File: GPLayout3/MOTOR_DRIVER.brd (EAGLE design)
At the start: 169.2 x 45.4 mm, 95 parts, among them T1 2N2222, T2 2N2222, U7 ATMEGA328P_TQFP, Y1 16MHz

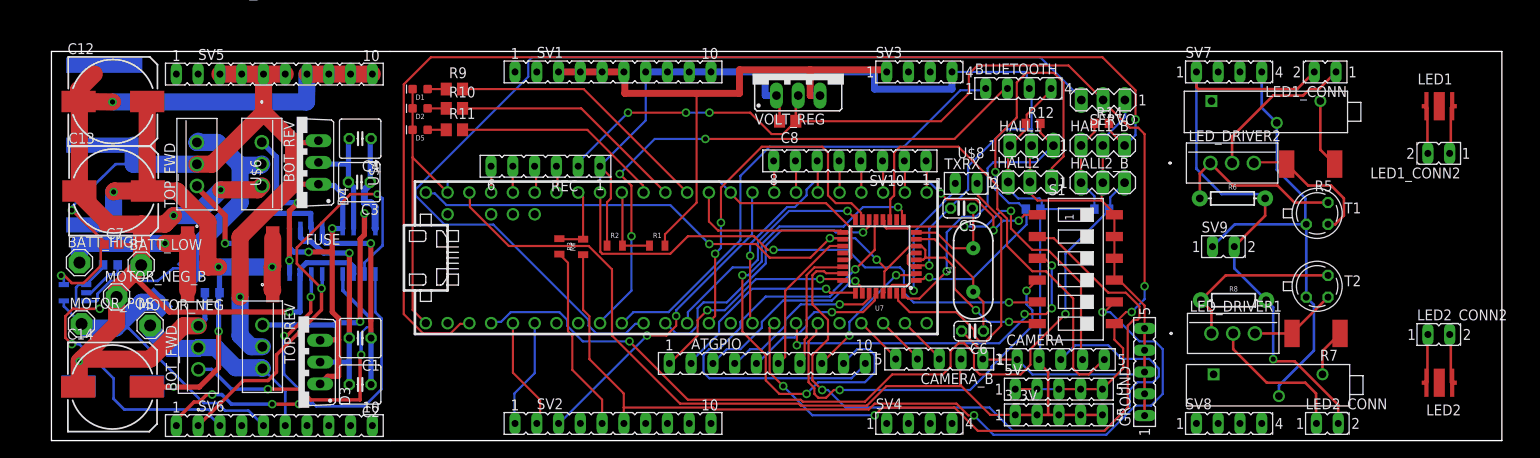
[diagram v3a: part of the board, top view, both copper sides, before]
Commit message: added several resistor values
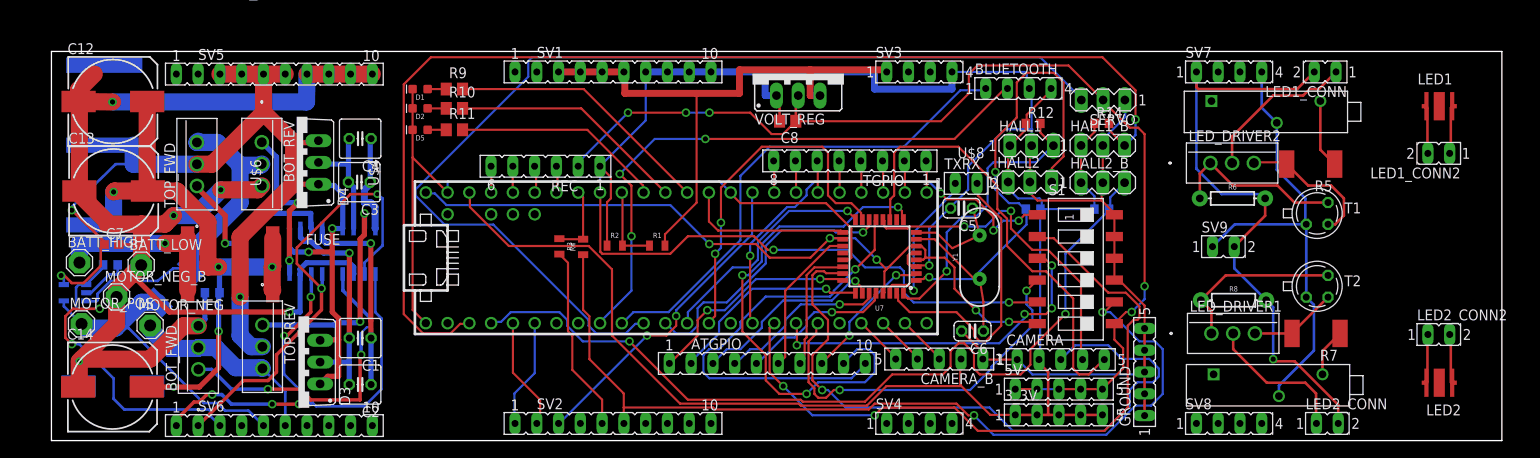
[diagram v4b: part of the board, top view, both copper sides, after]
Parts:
- R10, R11, R9: value (none) -> 59
- R5, R7: value (none) -> 1
- moved Y1 1.68 mm to (108.3, 21.4)
- renumbered SV10 to TGPIO
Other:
- outline, holes or cut-outs redrawn
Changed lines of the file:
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@@
 <?xml version="1.0" encoding="utf-8"?>
 <!DOCTYPE eagle SYSTEM "eagle.dtd">
-<eagle version="8.0.0">
+<eagle version="8.0.1">
 <drawing>
 <settings>
@@
 <board>
 <plain>
-<wire x1="0" y1="0" x2="39.5" y2="0" width="0" layer="20"/>
-<wire x1="39.5" y1="0" x2="169.17" y2="0" width="0" layer="20"/>
+<wire x1="0" y1="0" x2="169.17" y2="0" width="0" layer="20"/>
 <wire x1="169.17" y1="0" x2="169.17" y2="45.39" width="0" layer="20"/>
-<wire x1="169.17" y1="45.39" x2="39.5" y2="45.39" width="0" layer="20"/>
+<wire x1="169.17" y1="45.39" x2="0" y2="45.39" width="0" layer="20"/>
 <dimension x1="39.5" y1="0" x2="130.94" y2="0" x3="85.22" y3="-29.21" textsize="1.778" layer="48" unit="inch"/>
-<wire x1="39.5" y1="45.39" x2="0" y2="45.39" width="0" layer="20"/>
 <wire x1="0" y1="45.39" x2="0" y2="0" width="0" layer="20"/>
 <dimension x1="1" y1="45.54" x2="1" y2="-0.18" x3="-6.62" y3="22.68" textsize="1.778" layer="48" unit="inch"/>
@@
 <attribute name="PRICE" value="$1.38" x="96.578" y="21.482" size="1.778" layer="27" rot="R180" display="off"/>
 </element>
-<element name="Y1" library="SparkFun-Clocks" package="HC49US" value="16MHz" x="107.515" y="19.9" rot="R90">
-<attribute name="DIGIKEY_PART_NUMBER" value="887-2425-1-ND" x="107.515" y="19.9" size="1.778" layer="27" rot="R90" display="off"/>
-<attribute name="MANUFACTURER" value="TXC CORPORATION" x="107.515" y="19.9" size="1.778" layer="27" rot="R90" display="off"/>
-<attribute name="MANUFACTURER_PART_NUMBER" value="9C-16.000MBBK-T" x="107.515" y="19.9" size="1.778" layer="27" rot="R90" display="off"/>
-<attribute name="PRICE" value="$0.36" x="107.515" y="19.9" size="1.778" layer="27" rot="R90" display="off"/>
+<element name="Y1" library="SparkFun-Clocks" package="HC49US" value="16MHz" x="108.265" y="21.4" rot="R90">
+<attribute name="DIGIKEY_PART_NUMBER" value="887-2425-1-ND" x="108.265" y="21.4" size="1.778" layer="27" rot="R90" display="off"/>
+<attribute name="MANUFACTURER" value="TXC CORPORATION" x="108.265" y="21.4" size="1.778" layer="27" rot="R90" display="off"/>
+<attribute name="MANUFACTURER_PART_NUMBER" value="9C-16.000MBBK-T" x="108.265" y="21.4" size="1.778" layer="27" rot="R90" display="off"/>
+<attribute name="PRICE" value="$0.36" x="108.265" y="21.4" size="1.778" layer="27" rot="R90" display="off"/>
 </element>
 <element name="SV1" library="con-lsta" package="FE10" value="" x="65.5" y="43"/>
@@
 </element>
 <element name="U$7" library="ledpot" package="POT" value="POT" x="132.125" y="40.75" rot="R270"/>
-<element name="R5" library="rcl" package="R2512" value="" x="146.875" y="32.25" rot="R180"/>
+<element name="R5" library="rcl" package="R2512" value="1" x="146.875" y="32.25" rot="R180"/>
 <element name="T1" library="transistor" package="TO18" value="2N2222" x="147.625" y="26.5"/>
 <element name="R6" library="SparkFun-Resistors" package="AXIAL-0.3" value="1k" x="137.75" y="28.25">
@@
 </element>
 <element name="U$3" library="ledpot" package="POT" value="POT" x="132.375" y="8.875" rot="R270"/>
-<element name="R7" library="rcl" package="R2512" value="" x="147.5" y="12.5" rot="R180"/>
+<element name="R7" library="rcl" package="R2512" value="1" x="147.5" y="12.5" rot="R180"/>
 <element name="T2" library="transistor" package="TO18" value="2N2222" x="147.625" y="18"/>
 <element name="R8" library="SparkFun-Resistors" package="AXIAL-0.3" value="1k" x="137.875" y="16.375">
@@
 <element name="3_3V" library="con-lsta" package="FE05-1" value="" x="117.5" y="3"/>
 <element name="5V" library="con-lsta" package="FE05-1" value="" x="117.5" y="6"/>
-<element name="R9" library="rcl" package="R0805" value="" x="47" y="41"/>
-<element name="R10" library="rcl" package="R0805" value="" x="47" y="38.75"/>
-<element name="R11" library="rcl" package="R0805" value="" x="47" y="36.25"/>
+<element name="R9" library="rcl" package="R0805" value="59" x="47" y="41"/>
+<element name="R10" library="rcl" package="R0805" value="59" x="47" y="38.75"/>
+<element name="R11" library="rcl" package="R0805" value="59" x="47" y="36.25"/>
 <element name="D1" library="SparkFun-LED" package="LED-0603" value="" x="43" y="41" rot="R180"/>
 <element name="D2" library="SparkFun-LED" package="LED-0603" value="" x="43" y="38.75" rot="R180"/>
@@
 <element name="ATGPIO" library="con-lsta" package="FE10" value="" x="83.5" y="9"/>
 <element name="R17" library="rcl" package="R2512" value="10m" x="14.394540625" y="18.11175" rot="MR315"/>
-<element name="SV10" library="con-lsta" package="FE08" value="" x="93.125" y="32.625" rot="R180">
+<element name="TGPIO" library="con-lsta" package="FE08" value="" x="93.125" y="32.625" rot="R180">
 <attribute name="OC_NEWARK" value="unknown" x="93.125" y="32.625" size="1.778" layer="27" rot="R180" display="off"/>
 <attribute name="MF" value="" x="93.125" y="32.625" size="1.778" layer="27" rot="R180" display="off"/>
@@
 <contactref element="Y1" pad="1"/>
 <wire x1="108.7" y1="12.77" x2="108.7" y2="16.175" width="0.25" layer="1"/>
-<wire x1="108.7" y1="16.175" x2="107.515" y2="17.36" width="0.25" layer="1"/>
-<wire x1="107.515" y1="17.36" x2="107.515" y2="18.985" width="0.25" layer="1"/>
+<wire x1="108.7" y1="16.175" x2="108.265" y2="18.86" width="0.25" layer="1"/>
+<wire x1="108.265" y1="18.86" x2="107.515" y2="18.985" width="0.25" layer="1"/>
 <wire x1="107.515" y1="18.985" x2="103" y2="23.5" width="0.25" layer="1"/>
 <wire x1="103" y1="23.5" x2="100.8886" y2="23.5" width="0.25" layer="1"/>
@@
 <contactref element="Y1" pad="2"/>
 <contactref element="U7" pad="8"/>
-<wire x1="107.515" y1="27.01" x2="107.515" y2="22.44" width="0.25" layer="1"/>
+<wire x1="107.515" y1="27.01" x2="108.265" y2="23.94" width="0.25" layer="1"/>
 <wire x1="107.515" y1="27.01" x2="107.415" y2="27.11" width="0.25" layer="1"/>
-<wire x1="107.515" y1="22.44" x2="105.06" y2="22.44" width="0.25" layer="1"/>
+<wire x1="108.265" y1="23.94" x2="105.06" y2="22.44" width="0.25" layer="1"/>
 <wire x1="105.06" y1="22.44" x2="103.25" y2="24.25" width="0.25" layer="1"/>
 <wire x1="103.25" y1="24.25" x2="100.9026" y2="24.25" width="0.25" layer="1"/>
@@
 <signal name="TGPIO1">
 <contactref element="U$1" pad="33/A14"/>
-<contactref element="SV10" pad="1"/>
+<contactref element="TGPIO" pad="1"/>
 <wire x1="102.084" y1="28.938" x2="102.084" y2="32.556" width="0.25" layer="1"/>
 <wire x1="102.084" y1="32.556" x2="102.015" y2="32.625" width="0.25" layer="1"/>
@@
 <signal name="TGPIO2">
 <contactref element="U$1" pad="34/A15"/>
-<contactref element="SV10" pad="2"/>
+<contactref element="TGPIO" pad="2"/>
 <wire x1="99.544" y1="28.938" x2="99.544" y2="32.556" width="0.25" layer="1"/>
 <wire x1="99.544" y1="32.556" x2="99.475" y2="32.625" width="0.25" layer="1"/>
@@
 <signal name="TGPIO3">
 <contactref element="U$1" pad="35/A16"/>
-<contactref element="SV10" pad="3"/>
+<contactref element="TGPIO" pad="3"/>
 <wire x1="97.004" y1="28.938" x2="97.004" y2="32.556" width="0.25" layer="1"/>
 <wire x1="97.004" y1="32.556" x2="96.935" y2="32.625" width="0.25" layer="1"/>
@@
 <signal name="TGPIO4">
 <contactref element="U$1" pad="36/A17"/>
-<contactref element="SV10" pad="4"/>
+<contactref element="TGPIO" pad="4"/>
 <wire x1="94.464" y1="28.938" x2="94.464" y2="32.556" width="0.25" layer="1"/>
 <wire x1="94.464" y1="32.556" x2="94.395" y2="32.625" width="0.25" layer="1"/>
@@
 <signal name="TGPIO5">
 <contactref element="U$1" pad="37/A18"/>
-<contactref element="SV10" pad="5"/>
+<contactref element="TGPIO" pad="5"/>
 <wire x1="91.924" y1="28.938" x2="91.924" y2="32.556" width="0.25" layer="1"/>
 <wire x1="91.924" y1="32.556" x2="91.855" y2="32.625" width="0.25" layer="1"/>
@@
 <signal name="TGPIO6">
 <contactref element="U$1" pad="38/A19"/>
-<contactref element="SV10" pad="6"/>
+<contactref element="TGPIO" pad="6"/>
 <wire x1="89.384" y1="28.938" x2="89.384" y2="32.556" width="0.25" layer="1"/>
 <wire x1="89.384" y1="32.556" x2="89.315" y2="32.625" width="0.25" layer="1"/>
@@
 <signal name="TGPIO7">
 <contactref element="U$1" pad="39/A20"/>
-<contactref element="SV10" pad="7"/>
+<contactref element="TGPIO" pad="7"/>
 <wire x1="86.844" y1="28.938" x2="86.844" y2="32.556" width="0.25" layer="1"/>
 <wire x1="86.844" y1="32.556" x2="86.775" y2="32.625" width="0.25" layer="1"/>
@@
 <signal name="TGPIO8">
 <contactref element="U$1" pad="21/DAC0"/>
-<contactref element="SV10" pad="8"/>
+<contactref element="TGPIO" pad="8"/>
 <wire x1="84.304" y1="28.938" x2="84.304" y2="32.556" width="0.25" layer="1"/>
 <wire x1="84.304" y1="32.556" x2="84.235" y2="32.625" width="0.25" layer="1"/>

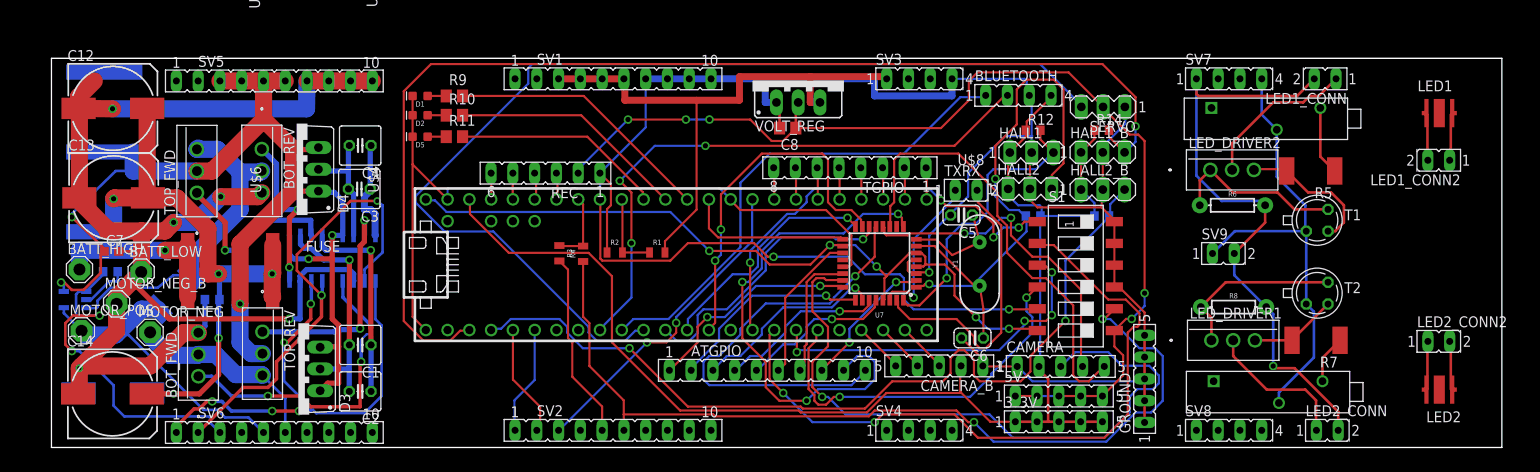
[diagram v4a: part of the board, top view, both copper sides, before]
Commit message: made overall dimensions smaller, moved I_SENSE and added back a GPIO. made an attempt at a gerber file
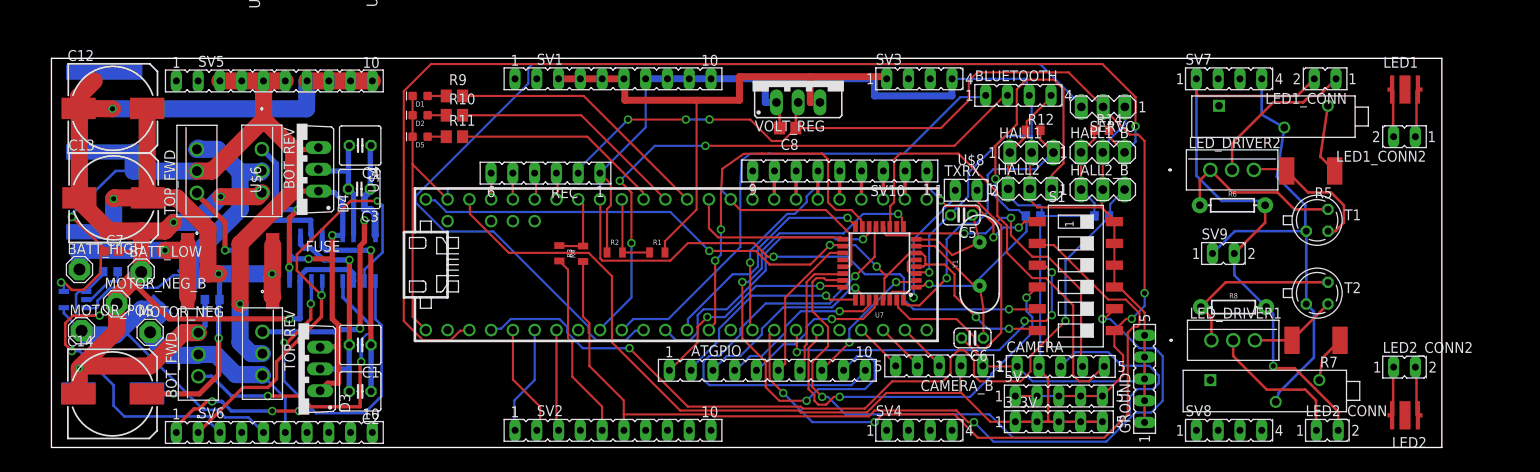
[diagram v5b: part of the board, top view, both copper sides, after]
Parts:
- removed TGPIO: (no value), con-lsta:FE08
- added SV10: (no value), con-lsta:FE09
- moved LED2 5.00 mm to (157.9, 3.75)
- moved LED2_CONN2 5.00 mm to (161.6, 9.38)
- moved LED1 4.85 mm to (157.9, 41.8)
- moved LED1_CONN2 4.85 mm to (154.0, 36.2)
- moved U$7 0.91 mm to (133.0, 41.0)
- moved U$3 0.40 mm to (132.0, 9.00)
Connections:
- removed net HI2: U$1.5
- new net TGPIO9: SV10.9, U$1.A22/DAC1
- net I_SENSE: now also U$1.5; no longer U$1.A22/DAC1
- net TGPIO1: now also SV10.1; no longer TGPIO.1
- net TGPIO2: now also SV10.2; no longer TGPIO.2
- net TGPIO3: now also SV10.3; no longer TGPIO.3
- net TGPIO4: now also SV10.4; no longer TGPIO.4
- net TGPIO5: now also SV10.5; no longer TGPIO.5
- net TGPIO6: now also SV10.6; no longer TGPIO.6
- net TGPIO7: now also SV10.7; no longer TGPIO.7
- net TGPIO8: now also SV10.8; no longer TGPIO.8
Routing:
- net I_SENSE: track 37.6 -> 11.8 mm, vias 2 -> 0
- net TGPIO9: track 0.00 -> 3.31 mm
- net SPI_MOSI: track 41.7 -> 43.1 mm
- net BLT_RX: track 58.3 -> 59.6 mm
- net GND_TOP2: track 54.0 -> 54.8 mm
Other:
- board size 169.2 x 45.4 mm -> 162.2 x 45.4 mm

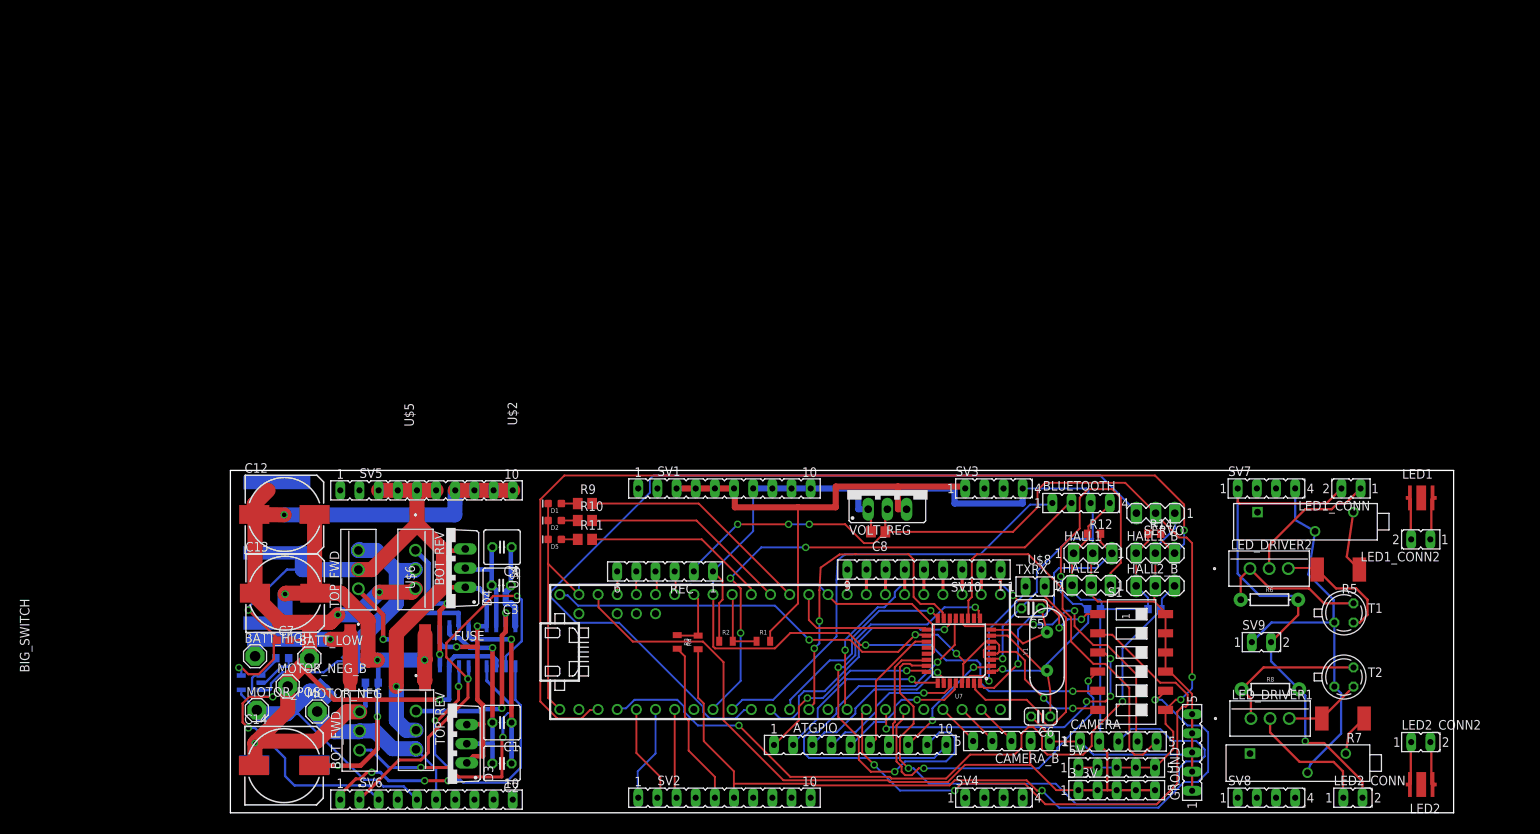
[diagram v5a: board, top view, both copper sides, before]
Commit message: Added silkscreen for most headers
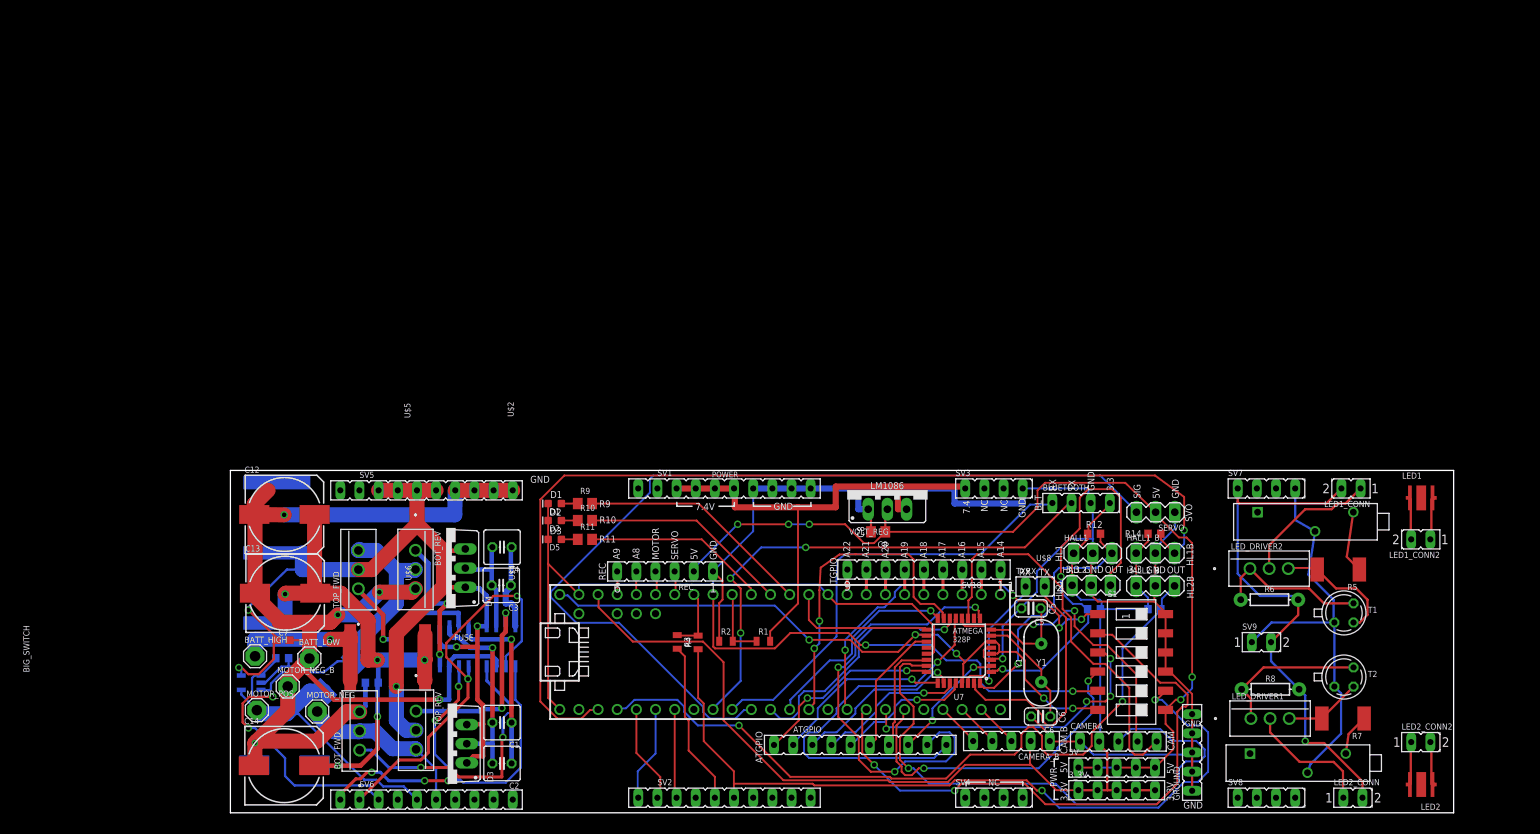
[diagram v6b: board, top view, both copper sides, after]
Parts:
- moved Y1 1.70 mm to (107.5, 19.9)
- moved SERVO 0.13 mm to (122.7, 39.9)
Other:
- board text added: "3.3"
- board text added: "3.3V"
- board text added: "5V"
- board text added: "7.4"
- board text added: "7.4V"
- board text added: "A14"
- board text added: "A15"
- board text added: "A16"
- board text added: "A17"
- board text added: "A18"
- board text added: "A19"
- board text added: "A20"
- board text added: "A21"
- board text added: "A22"
- board text added: "A8"
- board text added: "A9"
- board text added: "ATGPIO"
- board text added: "ATMEGA 328P"
- board text added: "BLT"
- board text added: "C5"
- board text added: "C6"
- board text added: "C8"
- board text added: "CAM"
- board text added: "CAM.B"
- board text added: "D1"
- board text added: "D2"
- board text added: "D3"
- board text added: "GND"
- board text added: "HL1"
- board text added: "HL1B"
- board text added: "HL2"
- board text added: "HL2B"
- board text added: "LM1086"
- board text added: "MOTOR"
- board text added: "NC"
- board text added: "OUT"
- board text added: "POWER"
- board text added: "PWR"
- board text added: "R10"
- board text added: "R11"
- board text added: "R9"
- board text added: "REC"
- board text added: "RX"
- board text added: "SERVO"
- board text added: "SIG"
- board text added: "SVO"
- board text added: "TGPIO"
- board text added: "TX"
- board text added: "Y1"
